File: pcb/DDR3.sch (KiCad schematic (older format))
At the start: 4 parts, among them U401 XC7Axxt-FGG484, U501 DDR3-x16

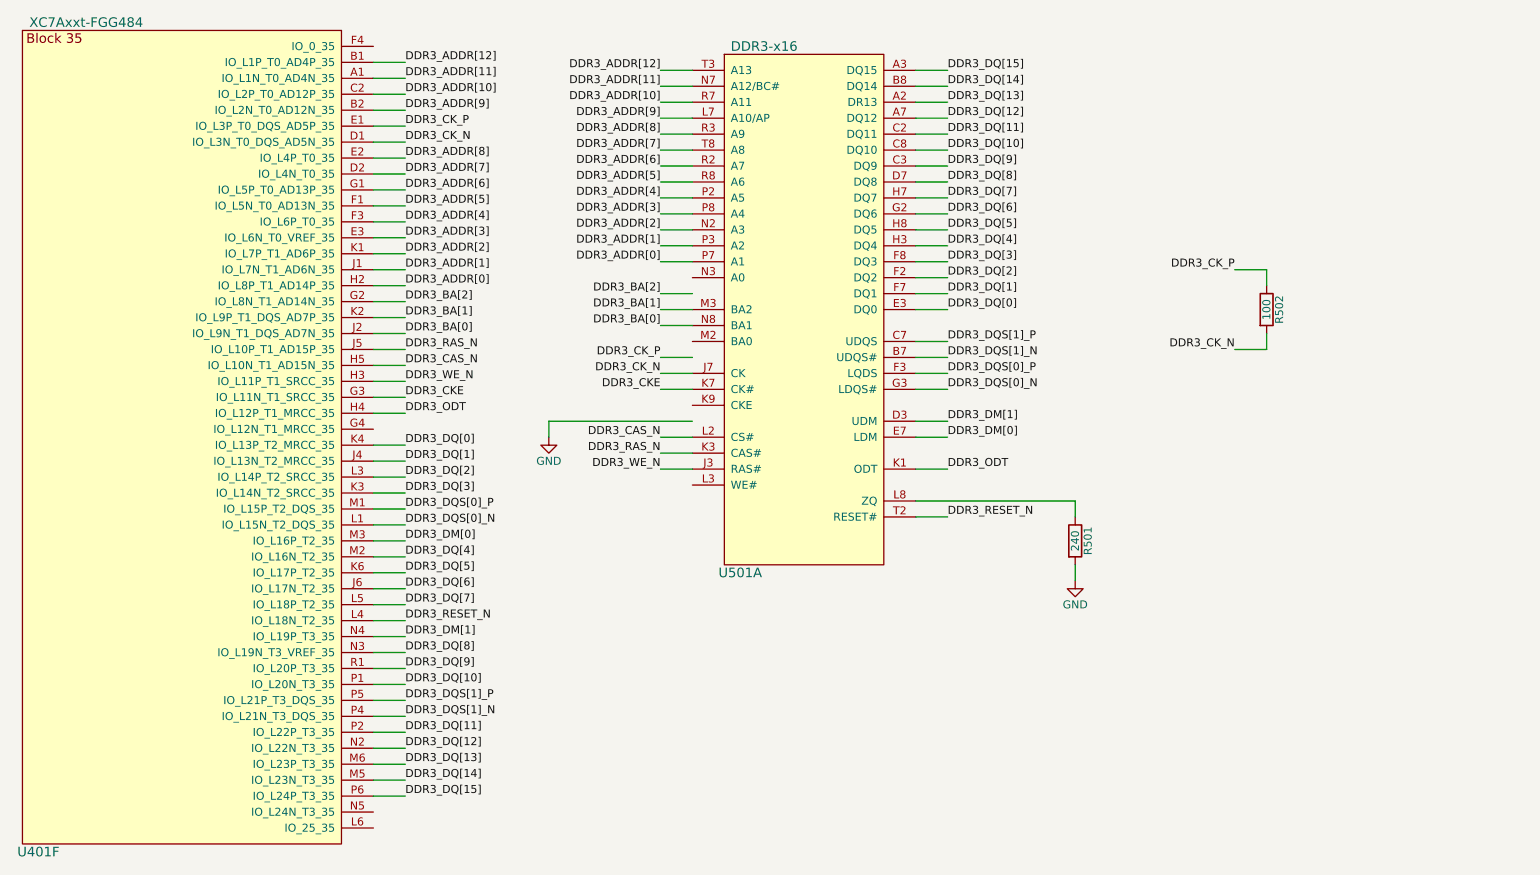
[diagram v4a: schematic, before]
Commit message: DDR routing test 1
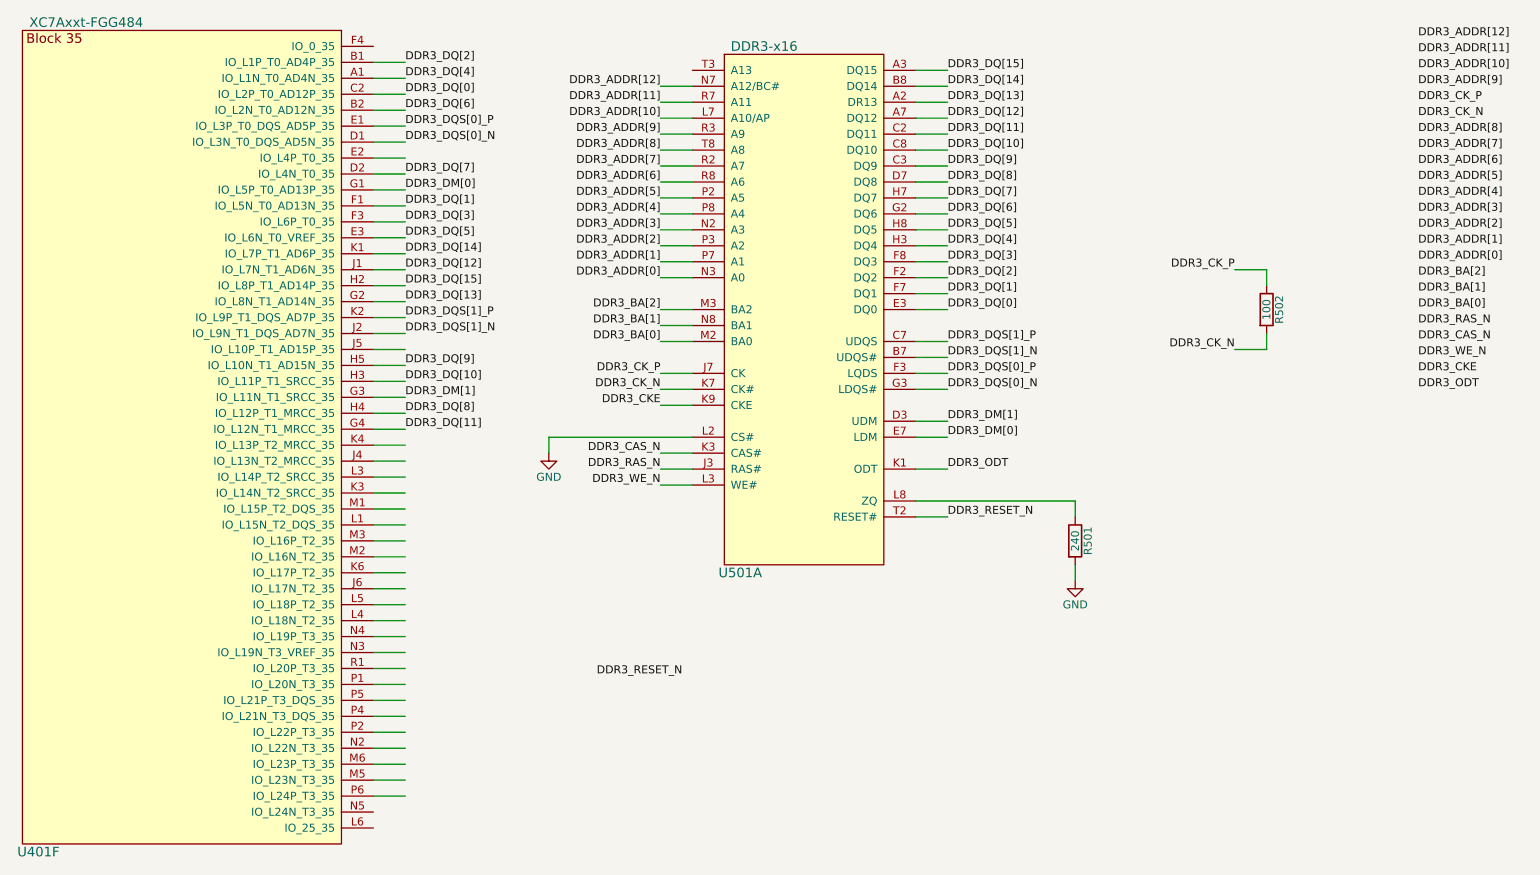
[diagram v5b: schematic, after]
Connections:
- wire segments 101 -> 102
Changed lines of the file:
@@
 $Descr A4 11693 8268
 encoding utf-8
-Sheet 5 12
+Sheet 5 13
 Title ""
 Date ""
@@
 Wire Wire Line
 	3400 5700 3600 5700
-Text Label 3600 3500 0    50   ~ 0
+Text Label 3600 1300 0    50   ~ 0
 DDR3_DQ[0]
-Text Label 3600 3600 0    50   ~ 0
+Text Label 3600 2000 0    50   ~ 0
 DDR3_DQ[1]
-Text Label 3600 3700 0    50   ~ 0
+Text Label 3600 1100 0    50   ~ 0
 DDR3_DQ[2]
-Text Label 3600 3800 0    50   ~ 0
+Text Label 3600 2100 0    50   ~ 0
 DDR3_DQ[3]
-Text Label 3600 4200 0    50   ~ 0
+Text Label 3600 1200 0    50   ~ 0
 DDR3_DQ[4]
-Text Label 3600 4300 0    50   ~ 0
+Text Label 3600 2200 0    50   ~ 0
 DDR3_DQ[5]
-Text Label 3600 4400 0    50   ~ 0
+Text Label 3600 1400 0    50   ~ 0
 DDR3_DQ[6]
-Text Label 3600 4500 0    50   ~ 0
+Text Label 3600 1800 0    50   ~ 0
 DDR3_DQ[7]
-Text Label 3600 4800 0    50   ~ 0
+Text Label 3600 3300 0    50   ~ 0
 DDR3_DQ[8]
-Text Label 3600 4900 0    50   ~ 0
+Text Label 3600 3000 0    50   ~ 0
 DDR3_DQ[9]
-Text Label 3600 5000 0    50   ~ 0
+Text Label 3600 3100 0    50   ~ 0
 DDR3_DQ[10]
-Text Label 3600 5300 0    50   ~ 0
+Text Label 3600 3400 0    50   ~ 0
 DDR3_DQ[11]
-Text Label 3600 5400 0    50   ~ 0
+Text Label 3600 2400 0    50   ~ 0
 DDR3_DQ[12]
-Text Label 3600 5500 0    50   ~ 0
+Text Label 3600 2600 0    50   ~ 0
 DDR3_DQ[13]
-Text Label 3600 5600 0    50   ~ 0
+Text Label 3600 2300 0    50   ~ 0
 DDR3_DQ[14]
-Text Label 3600 5700 0    50   ~ 0
+Text Label 3600 2500 0    50   ~ 0
 DDR3_DQ[15]
-Text Label 3600 1100 0    50   ~ 0
+Text Label 9950 950  0    50   ~ 0
 DDR3_ADDR[12]
-Text Label 3600 1200 0    50   ~ 0
+Text Label 9950 1050 0    50   ~ 0
 DDR3_ADDR[11]
-Text Label 3600 1300 0    50   ~ 0
+Text Label 9950 1150 0    50   ~ 0
 DDR3_ADDR[10]
-Text Label 3600 1400 0    50   ~ 0
+Text Label 9950 1250 0    50   ~ 0
 DDR3_ADDR[9]
-Text Label 3600 1700 0    50   ~ 0
+Text Label 9950 1550 0    50   ~ 0
 DDR3_ADDR[8]
-Text Label 3600 1800 0    50   ~ 0
+Text Label 9950 1650 0    50   ~ 0
 DDR3_ADDR[7]
+Text Label 9950 1750 0    50   ~ 0
+DDR3_ADDR[6]
+Text Label 9950 1850 0    50   ~ 0
+DDR3_ADDR[5]
+Text Label 9950 1950 0    50   ~ 0
+DDR3_ADDR[4]
+Text Label 9950 2050 0    50   ~ 0
+DDR3_ADDR[3]
+Text Label 9950 2150 0    50   ~ 0
+DDR3_ADDR[2]
+Text Label 9950 2250 0    50   ~ 0
+DDR3_ADDR[1]
+Text Label 9950 2350 0    50   ~ 0
+DDR3_ADDR[0]
+Text Label 9950 2450 0    50   ~ 0
+DDR3_BA[2]
+Text Label 9950 2550 0    50   ~ 0
+DDR3_BA[1]
+Text Label 9950 2650 0    50   ~ 0
+DDR3_BA[0]
+Text Label 9950 2750 0    50   ~ 0
+DDR3_RAS_N
+Text Label 9950 2850 0    50   ~ 0
+DDR3_CAS_N
+Text Label 9950 2950 0    50   ~ 0
+DDR3_WE_N
+Text Label 4800 4950 0    50   ~ 0
+DDR3_RESET_N
+Text Label 9950 3050 0    50   ~ 0
+DDR3_CKE
+Text Label 9950 3150 0    50   ~ 0
+DDR3_ODT
 Text Label 3600 1900 0    50   ~ 0
-DDR3_ADDR[6]
-Text Label 3600 2000 0    50   ~ 0
-DDR3_ADDR[5]
-Text Label 3600 2100 0    50   ~ 0
-DDR3_ADDR[4]
-Text Label 3600 2200 0    50   ~ 0
-DDR3_ADDR[3]
-Text Label 3600 2300 0    50   ~ 0
-DDR3_ADDR[2]
-Text Label 3600 2400 0    50   ~ 0
-DDR3_ADDR[1]
-Text Label 3600 2500 0    50   ~ 0
-DDR3_ADDR[0]
-Text Label 3600 2600 0    50   ~ 0
-DDR3_BA[2]
+DDR3_DM[0]
+Text Label 3600 3200 0    50   ~ 0
+DDR3_DM[1]
+Text Label 3600 1500 0    50   ~ 0
+DDR3_DQS[0]_P
+Text Label 3600 1600 0    50   ~ 0
+DDR3_DQS[0]_N
 Text Label 3600 2700 0    50   ~ 0
-DDR3_BA[1]
+DDR3_DQS[1]_P
 Text Label 3600 2800 0    50   ~ 0
-DDR3_BA[0]
-Text Label 3600 2900 0    50   ~ 0
-DDR3_RAS_N
-Text Label 3600 3000 0    50   ~ 0
-DDR3_CAS_N
-Text Label 3600 3100 0    50   ~ 0
-DDR3_WE_N
-Text Label 3600 4600 0    50   ~ 0
-DDR3_RESET_N
-Text Label 3600 3200 0    50   ~ 0
-DDR3_CKE
-Text Label 3600 3300 0    50   ~ 0
-DDR3_ODT
-Text Label 3600 4100 0    50   ~ 0
-DDR3_DM[0]
-Text Label 3600 4700 0    50   ~ 0
-DDR3_DM[1]
-Text Label 3600 3900 0    50   ~ 0
-DDR3_DQS[0]_P
-Text Label 3600 4000 0    50   ~ 0
-DDR3_DQS[0]_N
-Text Label 3600 5100 0    50   ~ 0
-DDR3_DQS[1]_P
-Text Label 3600 5200 0    50   ~ 0
 DDR3_DQS[1]_N
-Text Label 3600 1500 0    50   ~ 0
+Text Label 9950 1350 0    50   ~ 0
 DDR3_CK_P
-Text Label 3600 1600 0    50   ~ 0
+Text Label 9950 1450 0    50   ~ 0
 DDR3_CK_N
 Wire Wire Line
@@
 	6800 3950 7000 3950
 Wire Wire Line
+	5400 3750 5200 3750
+Wire Wire Line
+	5400 1250 5200 1250
+Wire Wire Line
+	5400 1350 5200 1350
+Wire Wire Line
+	5400 1450 5200 1450
+Wire Wire Line
+	5400 1550 5200 1550
+Wire Wire Line
+	5400 1650 5200 1650
+Wire Wire Line
+	5400 1750 5200 1750
+Wire Wire Line
+	5400 1850 5200 1850
+Wire Wire Line
+	5400 1950 5200 1950
+Wire Wire Line
+	5400 2050 5200 2050
+Wire Wire Line
+	5400 2150 5200 2150
+Wire Wire Line
+	5400 2250 5200 2250
+Wire Wire Line
+	5400 2350 5200 2350
+Wire Wire Line
+	5400 2450 5200 2450
+Wire Wire Line
+	5400 2650 5200 2650
+Wire Wire Line
+	5400 2750 5200 2750
+Wire Wire Line
+	5400 2850 5200 2850
+Wire Wire Line
+	5400 3050 5200 3050
+Wire Wire Line
+	5400 3150 5200 3150
+Wire Wire Line
+	5400 3250 5200 3250
+Wire Wire Line
+	4500 3450 5400 3450
+Wire Wire Line
+	5400 3550 5200 3550
+Wire Wire Line
 	5400 3650 5200 3650
-Wire Wire Line
-	5400 1150 5200 1150
-Wire Wire Line
-	5400 1250 5200 1250
-Wire Wire Line
-	5400 1350 5200 1350
-Wire Wire Line
-	5400 1450 5200 1450
-Wire Wire Line
-	5400 1550 5200 1550
-Wire Wire Line
-	5400 1650 5200 1650
-Wire Wire Line
-	5400 1750 5200 1750
-Wire Wire Line
-	5400 1850 5200 1850
-Wire Wire Line
-	5400 1950 5200 1950
-Wire Wire Line
-	5400 2050 5200 2050
-Wire Wire Line
-	5400 2150 5200 2150
-Wire Wire Line
-	5400 2250 5200 2250
-Wire Wire Line
-	5400 2350 5200 2350
-Wire Wire Line
-	5400 2550 5200 2550
-Wire Wire Line
-	5400 2650 5200 2650
-Wire Wire Line
-	5400 2750 5200 2750
-Wire Wire Line
-	5400 2950 5200 2950
-Wire Wire Line
-	5400 3050 5200 3050
-Wire Wire Line
-	5400 3150 5200 3150
-Wire Wire Line
-	4500 3350 5400 3350
-Wire Wire Line
-	5400 3450 5200 3450
-Wire Wire Line
-	5400 3550 5200 3550
 Text Label 7000 1150 0    50   ~ 0
 DDR3_DQ[15]
@@
 Text Label 7000 2650 0    50   ~ 0
 DDR3_DQ[0]
-Text Label 5200 1150 2    50   ~ 0
+Text Label 5200 1250 2    50   ~ 0
 DDR3_ADDR[12]
-Text Label 5200 1250 2    50   ~ 0
+Text Label 5200 1350 2    50   ~ 0
 DDR3_ADDR[11]
-Text Label 5200 1350 2    50   ~ 0
+Text Label 5200 1450 2    50   ~ 0
 DDR3_ADDR[10]
-Text Label 5200 1450 2    50   ~ 0
+Text Label 5200 1550 2    50   ~ 0
 DDR3_ADDR[9]
-Text Label 5200 1550 2    50   ~ 0
+Text Label 5200 1650 2    50   ~ 0
 DDR3_ADDR[8]
-Text Label 5200 1650 2    50   ~ 0
+Text Label 5200 1750 2    50   ~ 0
 DDR3_ADDR[7]
-Text Label 5200 1750 2    50   ~ 0
+Text Label 5200 1850 2    50   ~ 0
 DDR3_ADDR[6]
-Text Label 5200 1850 2    50   ~ 0
+Text Label 5200 1950 2    50   ~ 0
 DDR3_ADDR[5]
-Text Label 5200 1950 2    50   ~ 0
+Text Label 5200 2050 2    50   ~ 0
 DDR3_ADDR[4]
-Text Label 5200 2050 2    50   ~ 0
+Text Label 5200 2150 2    50   ~ 0
 DDR3_ADDR[3]
-Text Label 5200 2150 2    50   ~ 0
+Text Label 5200 2250 2    50   ~ 0
 DDR3_ADDR[2]
-Text Label 5200 2250 2    50   ~ 0
+Text Label 5200 2350 2    50   ~ 0
 DDR3_ADDR[1]
-Text Label 5200 2350 2    50   ~ 0
+Text Label 5200 2450 2    50   ~ 0
 DDR3_ADDR[0]
-Text Label 5200 2550 2    50   ~ 0
+Text Label 5200 2650 2    50   ~ 0
 DDR3_BA[2]
-Text Label 5200 2650 2    50   ~ 0
+Text Label 5200 2750 2    50   ~ 0
 DDR3_BA[1]
-Text Label 5200 2750 2    50   ~ 0
+Text Label 5200 2850 2    50   ~ 0
 DDR3_BA[0]
+Text Label 5200 3250 2    50   ~ 0
+DDR3_CKE
+Text Label 5200 3050 2    50   ~ 0
+DDR3_CK_P
 Text Label 5200 3150 2    50   ~ 0
-DDR3_CKE
-Text Label 5200 2950 2    50   ~ 0
-DDR3_CK_P
-Text Label 5200 3050 2    50   ~ 0
 DDR3_CK_N
+Text Label 5200 3650 2    50   ~ 0
+DDR3_RAS_N
 Text Label 5200 3550 2    50   ~ 0
-DDR3_RAS_N
-Text Label 5200 3450 2    50   ~ 0
 DDR3_CAS_N
-Text Label 5200 3650 2    50   ~ 0
+Text Label 5200 3750 2    50   ~ 0
 DDR3_WE_N
 Text Label 7000 3650 0    50   ~ 0
@@
 L GND #PWR079
 U 1 1 561B38E8
-P 4500 3450
-F 0 "#PWR079" H 4500 3200 50  0001 C CNN
-F 1 "GND" H 4500 3300 50  0000 C CNN
-F 2 "" H 4500 3450 60  0000 C CNN
-F 3 "" H 4500 3450 60  0000 C CNN
-	1    4500 3450
+P 4500 3550
+F 0 "#PWR079" H 4500 3300 50  0001 C CNN
+F 1 "GND" H 4500 3400 50  0000 C CNN
+F 2 "" H 4500 3550 60  0000 C CNN
+F 3 "" H 4500 3550 60  0000 C CNN
+	1    4500 3550
 	1    0    0    -1
 $EndComp
@@
 $EndComp
 Wire Wire Line
-	4500 3350 4500 3450
+	4500 3450 4500 3550
 Wire Wire Line
 	7800 3850 7800 3950
@@
 Text Label 8800 2900 2    50   ~ 0
 DDR3_CK_N
+Wire Wire Line
+	3400 3400 3600 3400
 $EndSCHEMATC
